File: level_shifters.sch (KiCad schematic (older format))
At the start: 35 parts, among them P1 M-2X06-87759_M, Q1 MMBF4117, U20 CD40106BM96, U23 BC857BS-13-F, U24 BC857BS-13-F, U31 BC857BS-13-F, U5 NLSX3018DTR2G, X9 1365-10

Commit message: cleanup from Eagle import
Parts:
- removed JP6: PINHD-1X02_2.54-SMD, adc_dac_v1:1X02SMD, symbol adc_dac_v1-eagle-import:PINHD-1X02_2.54-SMD
- removed P1: M-2X06-87759_M, adc_dac_v1:87759-12_M, symbol adc_dac_v1-eagle-import:M-2X06-87759_M
- removed Q1: MMBF4117, adc_dac_v1:SOT23, symbol adc_dac_v1-eagle-import:MMBF4117
- removed R43, R45, R66, R68, R72, R74: 20k, adc_dac_v1:R0603, symbol adc_dac_v1-eagle-import:R-US_R0603
- removed R44, R46, R67, R69, R73, R75: 1k, adc_dac_v1:R0603, symbol adc_dac_v1-eagle-import:R-US_R0603
- removed R47, R48, R70, R71, R76, R77: 0, adc_dac_v1:R0603, symbol adc_dac_v1-eagle-import:R-US_R0603
- removed U20: CD40106BM96, adc_dac_v1:D14_TEX, symbol adc_dac_v1-eagle-import:CD40106BM96
- removed U23, U24, U31: BC857BS-13-F, adc_dac_v1:SOT-363___(US6)_TOS, symbol adc_dac_v1-eagle-import:HN1A01FU-YLFCT
- removed X9: 1365-10, adc_dac_v1:1365-10, symbol adc_dac_v1-eagle-import:1365-10
- R37, R38, R39, R40, R50, R51, R52: footprint adc_dac_v1:R0603 -> Resistor_SMD:R_0603_1608Metric; symbol adc_dac_v1-eagle-import:R-US_R0603 -> Device:R_US
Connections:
- net labels added: +1V8, +3V3
- net labels removed: -6V5, 3V3, LS_A, LS_B, LS_C, LS_D, LS_E, LS_F, LS_IN0, LS_IN1, LS_IN2, LS_IN3, LS_IN4, LS_IN5, LS_OUT0, LS_OUT1, LS_OUT2, LS_OUT3, LS_OUT4, LS_OUT5
- wire segments 155 -> 42
- no-connect marks 0 -> 3
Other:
- note removed: "0 - 3.3V CMOS \n(from FPGA)"
- note removed: "VSS - VDD\nto FET switches on analog board"

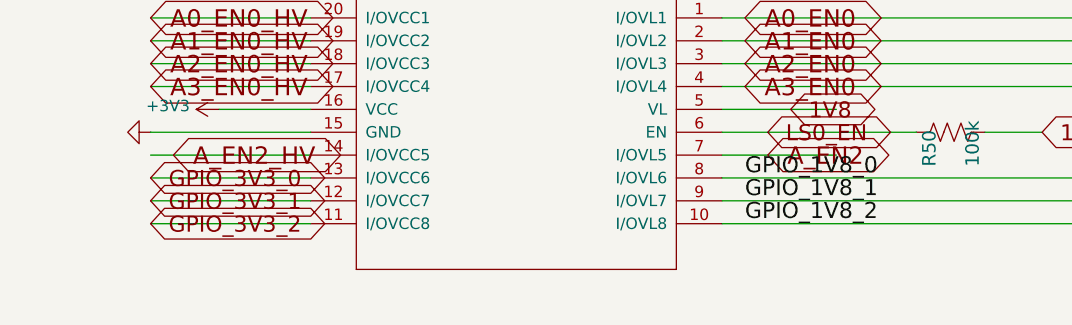
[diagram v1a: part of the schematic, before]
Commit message: updates to fast adc schematic
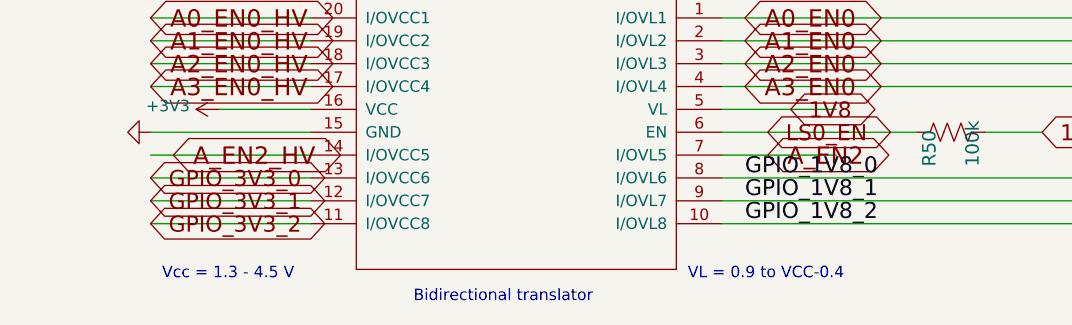
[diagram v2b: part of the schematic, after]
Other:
- note added: "Bidirectional translator"
- note added: "VL = 0.9 to VCC-0.4"
- note added: "Vcc = 1.3 - 4.5 V"
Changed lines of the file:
@@
 Text Notes 3800 2650 0    64   ~ 0
 These are global (for all ADC channels)\nEN0 is the only signal that needs FPGA control per ADC channel.
+Text Notes 6850 6450 0    50   ~ 0
+Bidirectional translator
+Text Notes 5750 6350 0    50   ~ 0
+Vcc = 1.3 - 4.5 V
+Text Notes 8050 6350 0    50   ~ 0
+VL = 0.9 to VCC-0.4
 $EndSCHEMATC

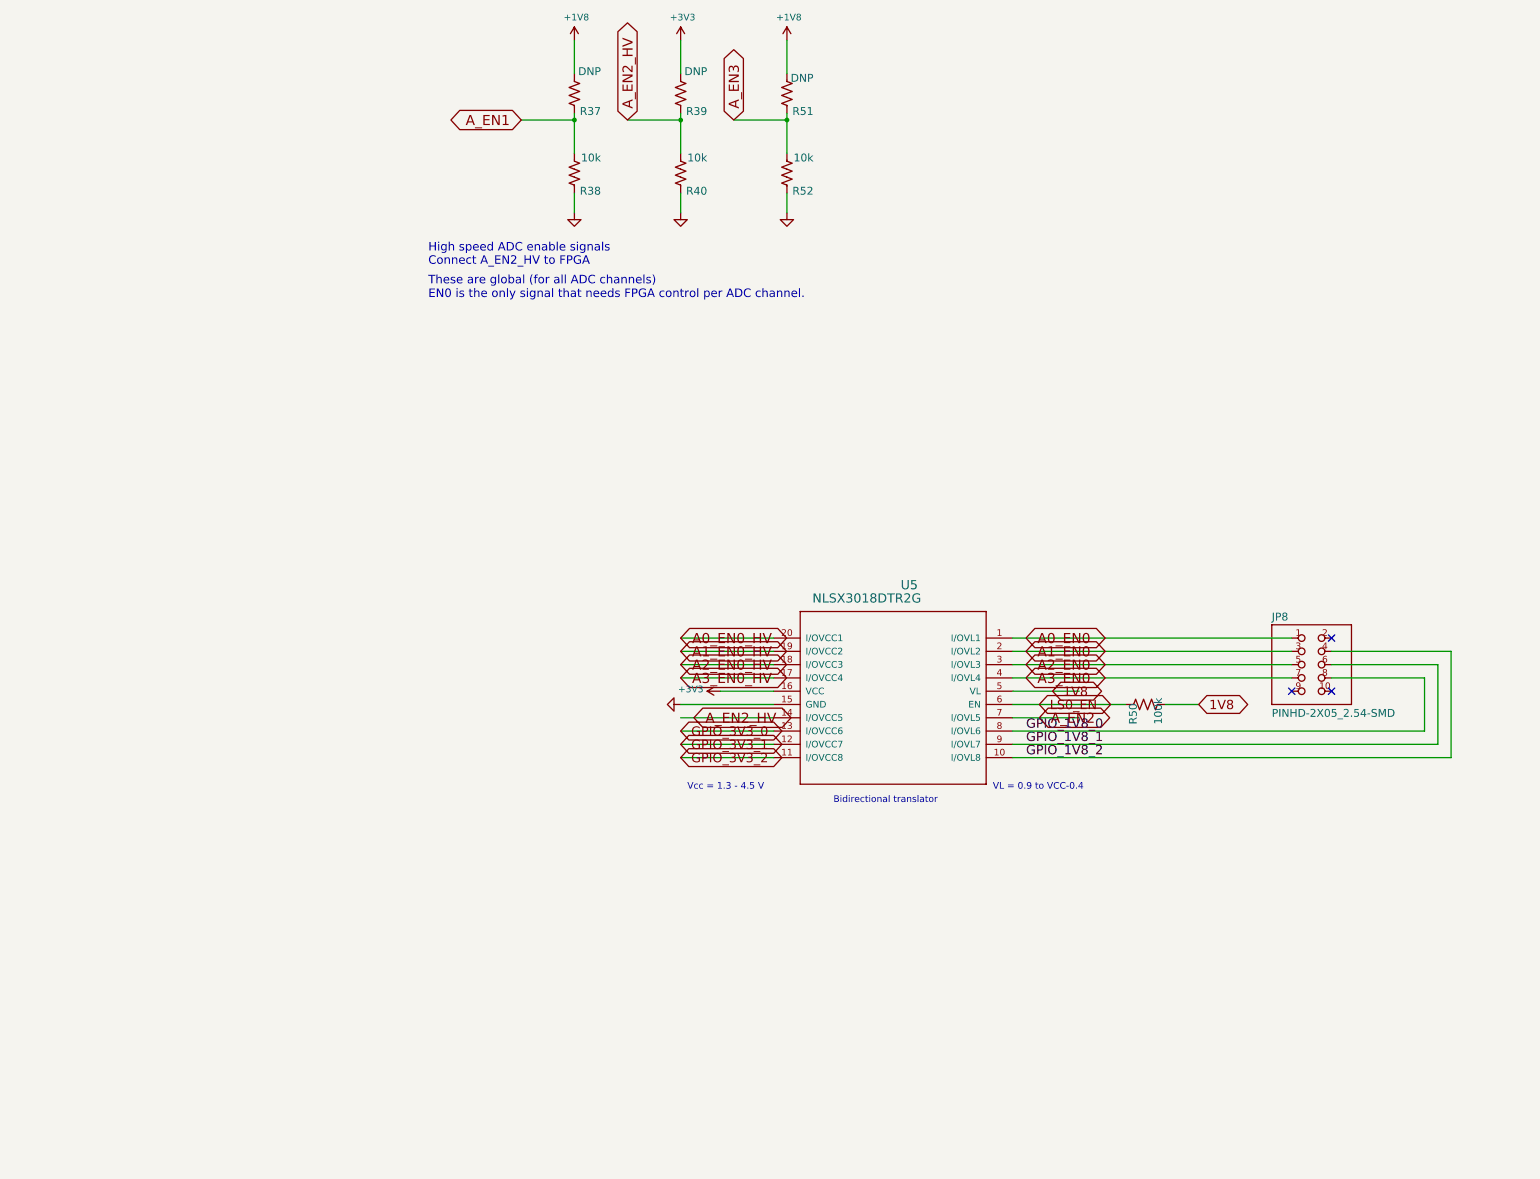
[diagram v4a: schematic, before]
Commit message: completed gp adc
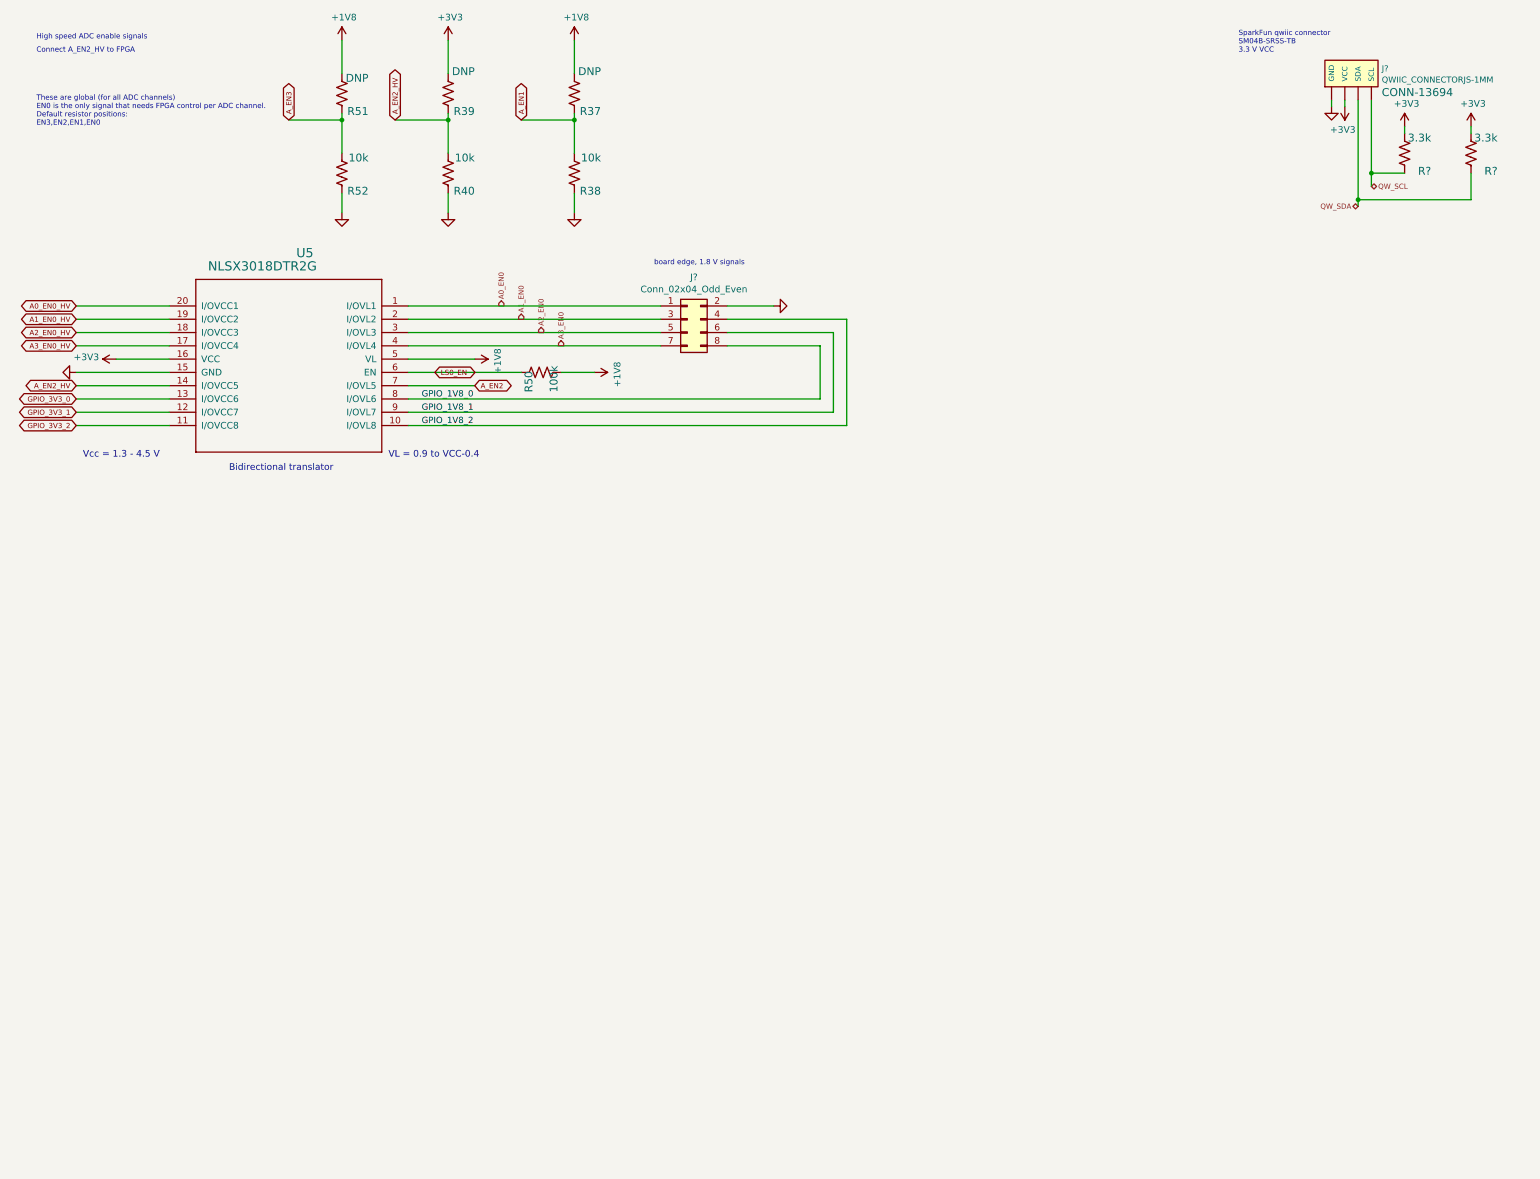
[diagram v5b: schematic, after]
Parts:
- removed JP8: PINHD-2X05_2.54-SMD, adc_dac_v1:2X05SMD, symbol adc_dac_v1-eagle-import:PINHD-2X05_2.54-SMD
- added J?: QWIIC_CONNECTORJS-1MM, 1X04_1MM_RA, symbol SparkFun-Connectors:QWIIC_CONNECTORJS-1MM
- added J?: Conn_02x04_Odd_Even, symbol Connector_Generic:Conn_02x04_Odd_Even
- added R? (x2): 3.3k, Resistor_SMD:R_0603_1608Metric, symbol Device:R_US
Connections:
- net labels added: QW_SCL, QW_SDA
- net labels removed: 1V8
- wire segments 42 -> 54
- no-connect marks 3 -> 0
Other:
- note added: "SparkFun qwiic connector\nSM04B-SRSS-TB\n3.3 V VCC"
- note added: "These are global (for all ADC channels)\nEN0 is the only signal that needs FPGA control per ADC channel.\nDefault resistor positions: \nEN3,EN2,EN1,EN0 \n0,0,0,FPGA (A_EN2_HV is high-Z)\n\ndriving EN2 high outputs test\npatterns on the LVDS interface"
- note added: "board edge, 1.8 V signals"
- note removed: "These are global (for all ADC channels)\nEN0 is the only signal that needs FPGA control per ADC channel."
- moved on the sheet: R39, R40, R50, R51, R52, U5

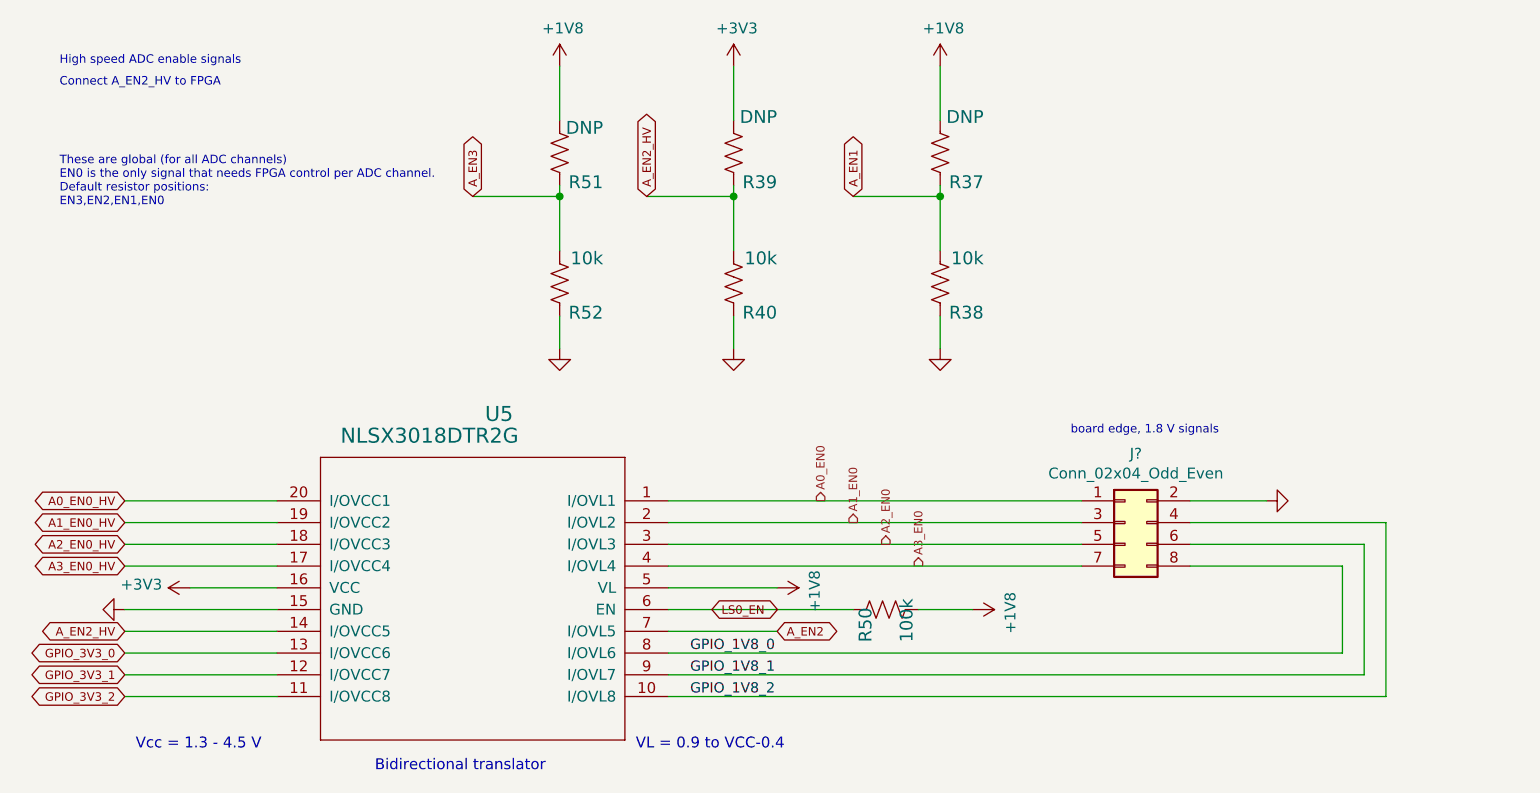
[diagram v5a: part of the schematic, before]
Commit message: modify LVDS connections for AD7960
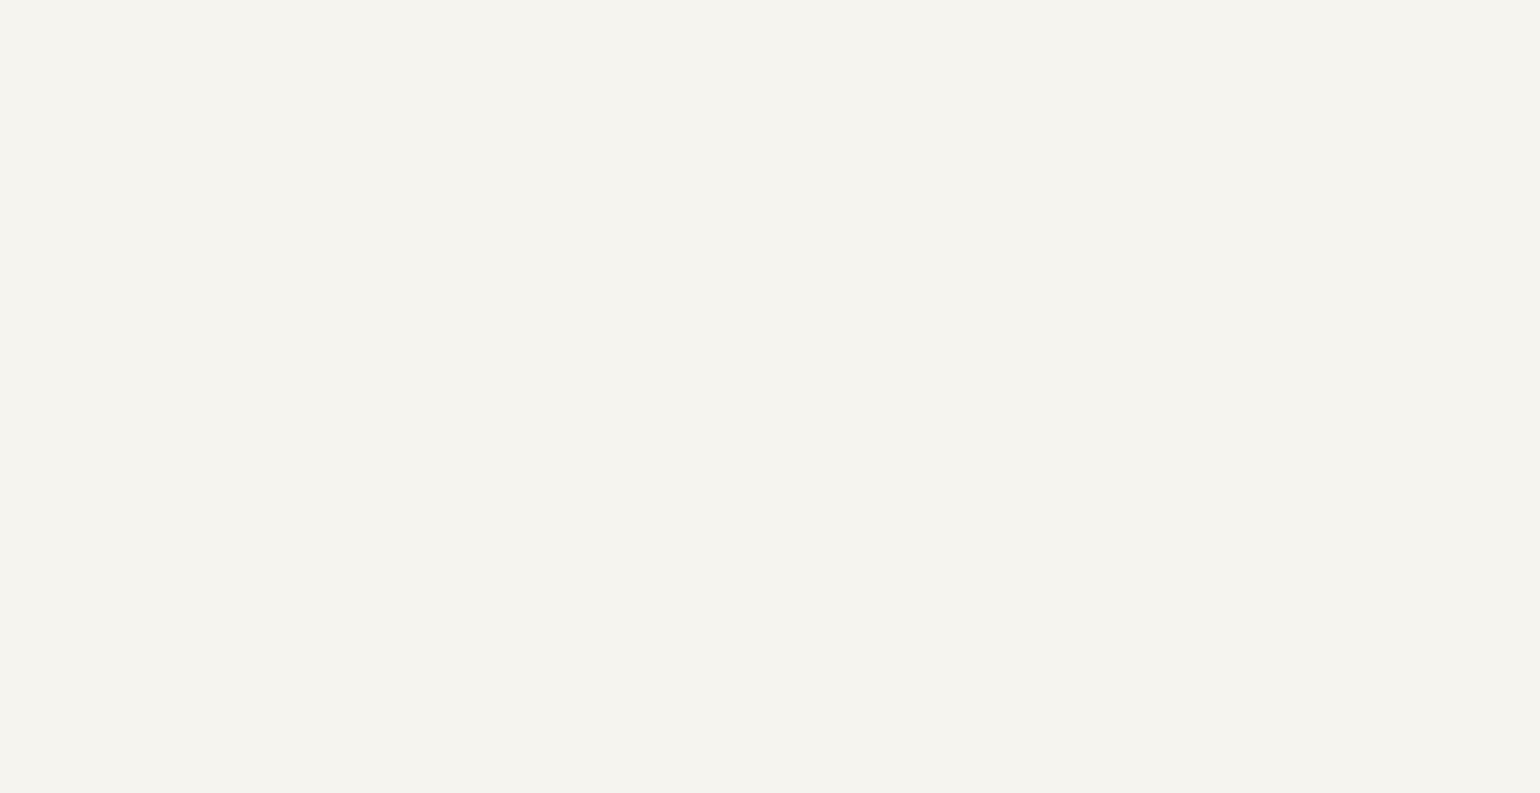
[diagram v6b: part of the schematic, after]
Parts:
- removed J?: Conn_02x04_Odd_Even, symbol Connector_Generic:Conn_02x04_Odd_Even
- removed R37, R39, R51: DNP, Resistor_SMD:R_0603_1608Metric, symbol Device:R_US
- removed R38, R40, R52: 10k, Resistor_SMD:R_0603_1608Metric, symbol Device:R_US
- removed R50: 100k, Resistor_SMD:R_0603_1608Metric, symbol Device:R_US
- removed U5: NLSX3018DTR2G, adc_dac_v1:TSSOP20_4P50X6P60_ONS, symbol adc_dac_v1-eagle-import:NLSX3018DTR2G
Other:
- note removed: "Bidirectional translator"
- note removed: "Connect A_EN2_HV to FPGA"
- note removed: "High speed ADC enable signals"
- note removed: "These are global (for all ADC channels)\nEN0 is the only signal that needs FPGA control per ADC channel.\nDefault resistor positions: \nEN3,EN2,EN1,EN0 \n0,0,0,FPGA (A_EN2_HV is high-Z)\n\ndriving EN2 high outputs test\npatterns on the LVDS interface"
- note removed: "VL = 0.9 to VCC-0.4"
- note removed: "Vcc = 1.3 - 4.5 V"
- note removed: "board edge, 1.8 V signals"

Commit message: moved level shifters to FPGA
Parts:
- removed J?: QWIIC_CONNECTORJS-1MM, 1X04_1MM_RA, symbol SparkFun-Connectors:QWIIC_CONNECTORJS-1MM
- removed R? (x2): 3.3k, Resistor_SMD:R_0603_1608Metric, symbol Device:R_US
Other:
- note removed: "SparkFun qwiic connector\nSM04B-SRSS-TB\n3.3 V VCC"
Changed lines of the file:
@@
 	1    0    0    -1
 $EndComp
-$Comp
-L SparkFun-Connectors:QWIIC_CONNECTORJS-1MM J?
-U 1 1 628A6C10
-P 10600 1050
-F 0 "J?" V 10463 1428 45  0000 L CNN
-F 1 "QWIIC_CONNECTORJS-1MM" V 10547 1428 45  0000 L CNN
-F 2 "1X04_1MM_RA" H 10600 1550 20  0001 C CNN
-F 3 "" H 10600 1050 50  0001 C CNN
-F 4 "CONN-13694" V 10642 1428 60  0000 L CNN "Field4"
-	1    10600 1050
-	0    1    1    0
-$EndComp
-Text Notes 9900 800  0    39   ~ 0
-SparkFun qwiic connector\nSM04B-SRSS-TB\n3.3 V VCC
-$Comp
-L power:GND #GND?
-U 1 1 628A8850
-P 10600 1200
-F 0 "#GND?" H 10600 1200 50  0001 C CNN
-F 1 "GND" H 10500 1100 59  0001 L BNN
-F 2 "" H 10600 1200 50  0001 C CNN
-F 3 "" H 10600 1200 50  0001 C CNN
-	1    10600 1200
-	1    0    0    -1
-$EndComp
-Wire Wire Line
-	10600 1200 10600 1150
-$Comp
-L power:+3V3 #PWR?
-U 1 1 628ABCDE
-P 10700 1200
-F 0 "#PWR?" H 10700 1050 50  0001 C CNN
-F 1 "+3V3" H 10715 1373 50  0000 C CNN
-F 2 "" H 10700 1200 50  0001 C CNN
-F 3 "" H 10700 1200 50  0001 C CNN
-	1    10700 1200
-	-1   0    0    1
-$EndComp
-Wire Wire Line
-	10700 1200 10700 1150
-Text HLabel 10900 1800 2    39   BiDi ~ 0
-QW_SCL
-Wire Wire Line
-	10800 1150 10800 1900
-Text HLabel 10800 1950 0    39   BiDi ~ 0
-QW_SDA
-$Comp
-L Device:R_US R?
-U 1 1 628AEF86
-P 11150 1550
-F 0 "R?" H 10950 1650 59  0000 L BNN
-F 1 "3.3k" H 10950 1400 59  0000 L BNN
-F 2 "Resistor_SMD:R_0603_1608Metric" H 11150 1550 50  0001 C CNN
-F 3 "RC0603FR-073K3L" H 11150 1550 50  0001 C CNN
-	1    11150 1550
-	-1   0    0    1
-$EndComp
-$Comp
-L power:+3V3 #PWR?
-U 1 1 628B3781
-P 11150 1350
-F 0 "#PWR?" H 11150 1200 50  0001 C CNN
-F 1 "+3V3" H 11165 1523 50  0000 C CNN
-F 2 "" H 11150 1350 50  0001 C CNN
-F 3 "" H 11150 1350 50  0001 C CNN
-	1    11150 1350
-	1    0    0    -1
-$EndComp
-Wire Wire Line
-	11150 1350 11150 1400
-Wire Wire Line
-	11150 1700 10900 1700
-Wire Wire Line
-	10900 1150 10900 1700
-Connection ~ 10900 1700
-Wire Wire Line
-	10900 1700 10900 1800
-$Comp
-L Device:R_US R?
-U 1 1 628CD44C
-P 11650 1550
-F 0 "R?" H 11450 1650 59  0000 L BNN
-F 1 "3.3k" H 11450 1400 59  0000 L BNN
-F 2 "Resistor_SMD:R_0603_1608Metric" H 11650 1550 50  0001 C CNN
-F 3 "RC0603FR-073K3L" H 11650 1550 50  0001 C CNN
-	1    11650 1550
-	-1   0    0    1
-$EndComp
-$Comp
-L power:+3V3 #PWR?
-U 1 1 628CD452
-P 11650 1350
-F 0 "#PWR?" H 11650 1200 50  0001 C CNN
-F 1 "+3V3" H 11665 1523 50  0000 C CNN
-F 2 "" H 11650 1350 50  0001 C CNN
-F 3 "" H 11650 1350 50  0001 C CNN
-	1    11650 1350
-	1    0    0    -1
-$EndComp
-Wire Wire Line
-	11650 1350 11650 1400
-Wire Wire Line
-	10800 1900 11650 1900
-Wire Wire Line
-	11650 1900 11650 1700
-Connection ~ 10800 1900
-Wire Wire Line
-	10800 1900 10800 1950
 $EndSCHEMATC
